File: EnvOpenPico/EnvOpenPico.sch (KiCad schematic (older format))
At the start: 40 parts, among them J2 SKRKAEE020, J3 2.54mm header 01x20, J4 2.54mm header 01x20, J5 Conn_01x03_Male, U1 TPS63002, U3 RP2040, X1 XO 32 12Mhz 3225 seiko

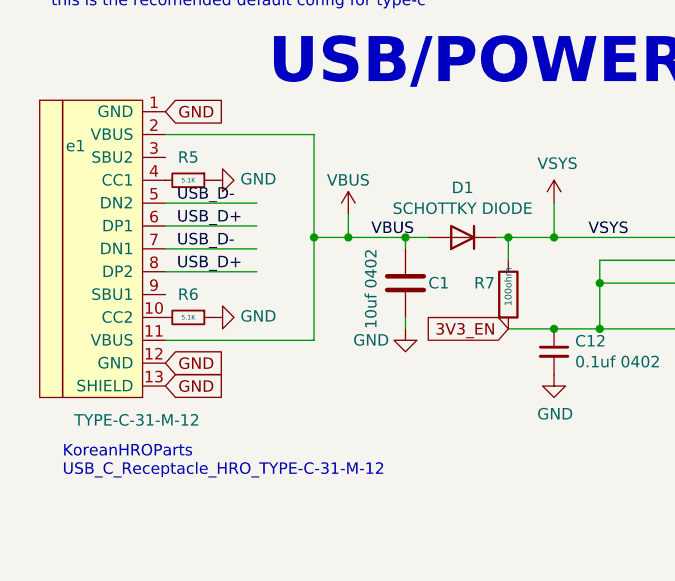
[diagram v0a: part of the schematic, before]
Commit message: small corrections and added a couple test points.
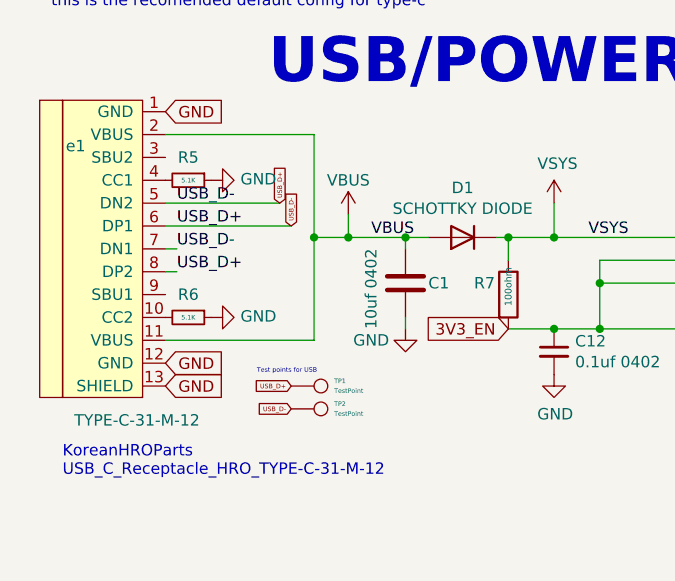
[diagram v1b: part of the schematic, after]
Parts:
- added TP1, TP2: TestPoint, TestPoint:TestPoint_Pad_1.0x1.0mm, symbol Connector:TestPoint
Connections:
- net USB_D- is gone; now on net USB_D+: R4.1, e1.5 (DN2), e1.7 (DN1)
- net USB_D+: now also TP1.1, TP2.1
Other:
- note added: "Test points for USB"
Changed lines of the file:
@@
 	1750 1300 1750 1750
 Connection ~ 1900 1750
-Wire Wire Line
-	1100 1600 1500 1600
-Wire Wire Line
-	1100 1700 1500 1700
 Text Label 1150 1900 0    50   ~ 0
 USB_D+
 Text Label 1150 1800 0    50   ~ 0
 USB_D-
-Wire Wire Line
-	1100 1800 1500 1800
-Wire Wire Line
-	1100 1900 1500 1900
 Wire Wire Line
 	1750 1750 1750 2200
@@
 Wire Wire Line
 	14600 5200 14100 5200
+Text GLabel 1600 1600 1    20   Input ~ 0
+USB_D+
+Text GLabel 1650 1700 1    20   Input ~ 0
+USB_D-
+Text GLabel 1650 2500 0    20   Input ~ 0
+USB_D-
+Text GLabel 1650 2400 0    20   Input ~ 0
+USB_D+
+$Comp
+L Connector:TestPoint TP1
+U 1 1 6102353C
+P 1650 2400
+F 0 "TP1" V 1628 2588 20  0000 L CNN
+F 1 "TestPoint" V 1671 2588 20  0000 L CNN
+F 2 "TestPoint:TestPoint_Pad_1.0x1.0mm" H 1850 2400 50  0001 C CNN
+F 3 "~" H 1850 2400 50  0001 C CNN
+	1    1650 2400
+	0    1    1    0
+$EndComp
+$Comp
+L Connector:TestPoint TP2
+U 1 1 61023F3F
+P 1650 2500
+F 0 "TP2" V 1628 2688 20  0000 L CNN
+F 1 "TestPoint" V 1671 2688 20  0000 L CNN
+F 2 "TestPoint:TestPoint_Pad_1.0x1.0mm" H 1850 2500 50  0001 C CNN
+F 3 "~" H 1850 2500 50  0001 C CNN
+	1    1650 2500
+	0    1    1    0
+$EndComp
+Wire Wire Line
+	1100 1600 1600 1600
+Wire Wire Line
+	1100 1700 1650 1700
+Wire Wire Line
+	1100 1800 1150 1800
+Wire Wire Line
+	1100 1900 1150 1900
+Text Notes 1500 2350 0    20   ~ 0
+Test points for USB
 $EndSCHEMATC

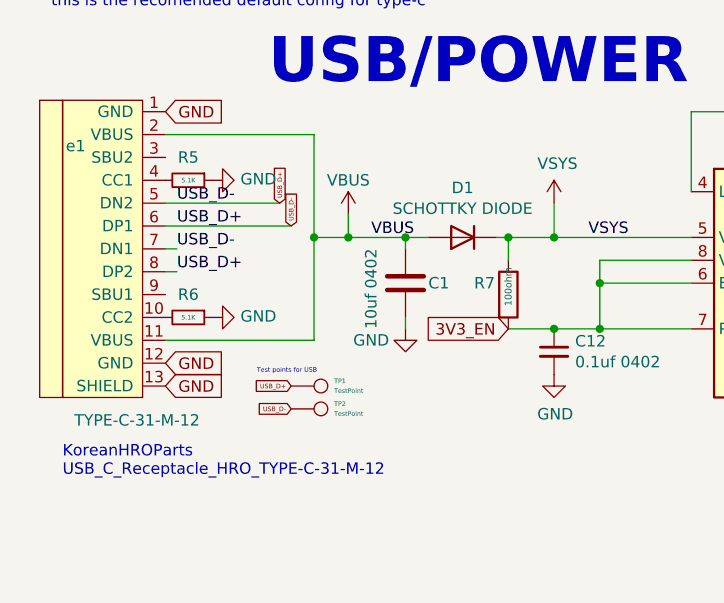
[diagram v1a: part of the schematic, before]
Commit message: corrected reveresed usb debug pads, added gnd debug pad and incremented revision number.
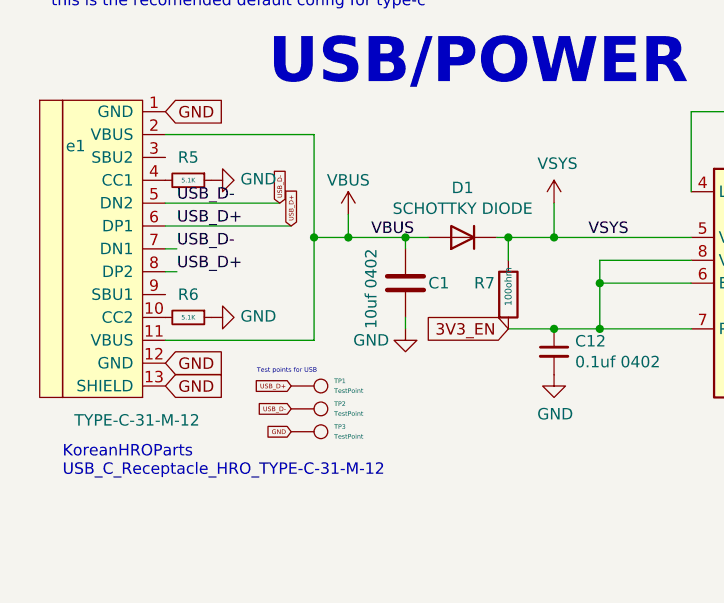
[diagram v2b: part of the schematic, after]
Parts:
- added TP3: TestPoint, TestPoint:TestPoint_Pad_1.0x1.0mm, symbol Connector:TestPoint
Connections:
- net GND: now also TP3.1
- net USB_D+: no longer R4.1, TP2.1, e1.5 (DN2), e1.7 (DN1)
- new net USB_D-: R4.1, TP2.1, e1.5 (DN2), e1.7 (DN1)
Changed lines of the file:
@@
 Wire Wire Line
 	14600 5200 14100 5200
+Text GLabel 1650 1700 1    20   Input ~ 0
+USB_D+
 Text GLabel 1600 1600 1    20   Input ~ 0
-USB_D+
-Text GLabel 1650 1700 1    20   Input ~ 0
 USB_D-
 Text GLabel 1650 2500 0    20   Input ~ 0
@@
 $EndComp
 Wire Wire Line
-	1100 1600 1600 1600
-Wire Wire Line
-	1100 1700 1650 1700
-Wire Wire Line
 	1100 1800 1150 1800
 Wire Wire Line
@@
 Text Notes 1500 2350 0    20   ~ 0
 Test points for USB
+$Comp
+L Connector:TestPoint TP3
+U 1 1 60FFE72F
+P 1650 2600
+F 0 "TP3" V 1628 2788 20  0000 L CNN
+F 1 "TestPoint" V 1671 2788 20  0000 L CNN
+F 2 "TestPoint:TestPoint_Pad_1.0x1.0mm" H 1850 2600 50  0001 C CNN
+F 3 "~" H 1850 2600 50  0001 C CNN
+	1    1650 2600
+	0    1    1    0
+$EndComp
+Text GLabel 1650 2600 0    20   Input ~ 0
+GND
+Wire Wire Line
+	1100 1600 1600 1600
+Wire Wire Line
+	1100 1700 1650 1700
 $EndSCHEMATC

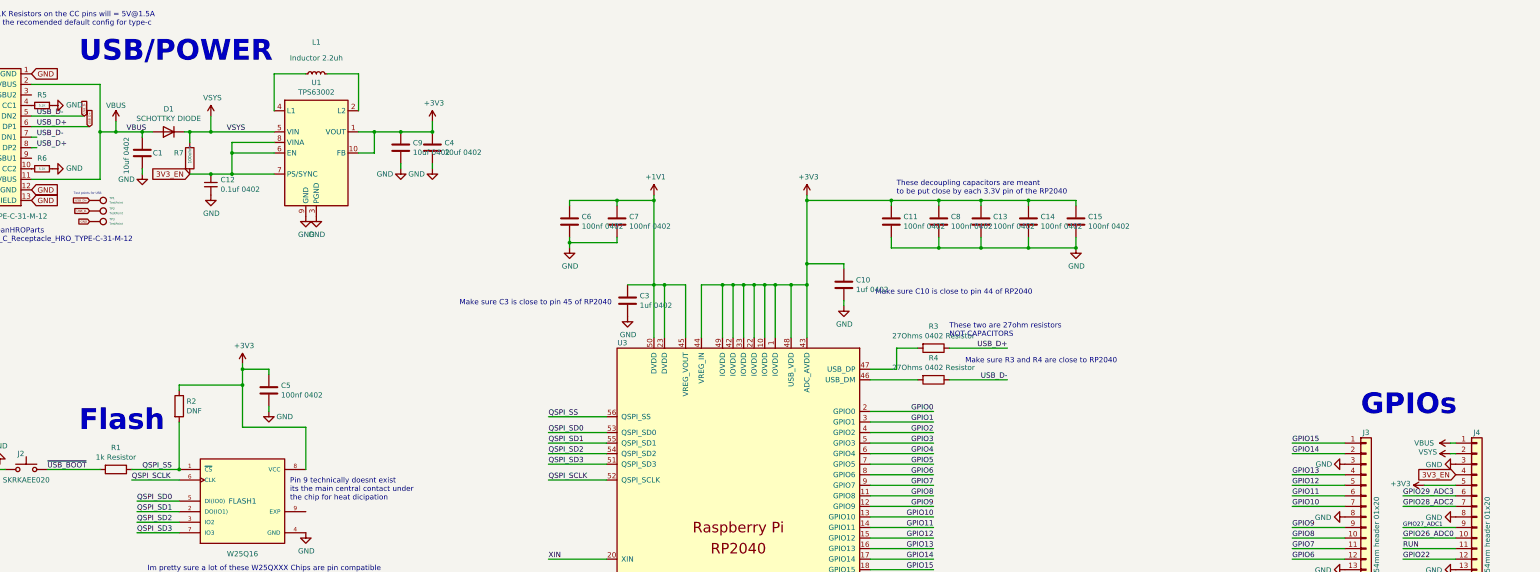
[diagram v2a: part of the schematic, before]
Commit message: Hopefully implemented ADC_VREF Correctly on dip40 and pico verrsion
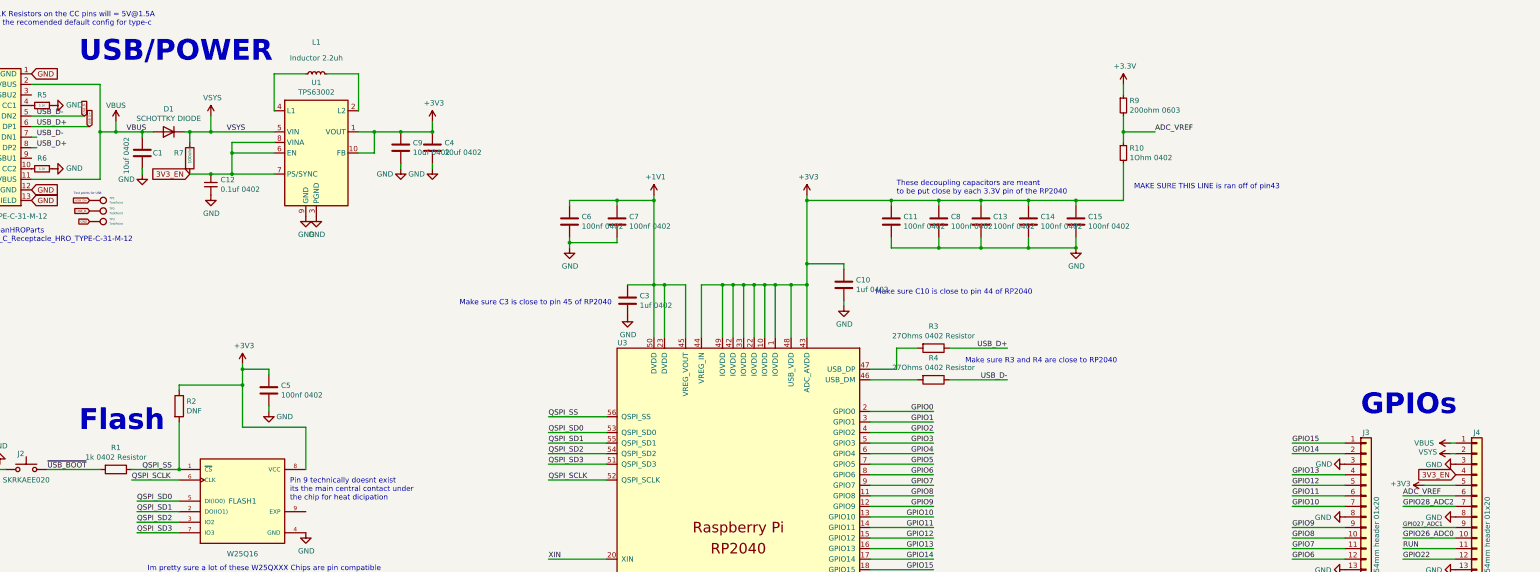
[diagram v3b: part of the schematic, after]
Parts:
- added R10: 1Ohm 0402, Resistor_SMD:R_0402_1005Metric, symbol Device:R_Small
- added R9: 200ohm 0603, Resistor_SMD:R_0603_1608Metric, symbol Device:R_Small
- R1: value 1k Resistor -> 1k 0402 Resistor
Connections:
- net +3V3: now also R10.2, R9.1
- net GPIO29_ADC3: no longer J4.6 (Pin_6)
- new net ADC_VREF: J4.6 (Pin_6), R10.1, R9.2
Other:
- note added: "MAKE SURE THIS LINE is ran off of pin43"
- note removed: "These two are 27ohm resistors \nNOT CAPACITORS"
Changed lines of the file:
@@
 P 1900 4950
 F 0 "R1" V 1693 4950 50  0000 C CNN
-F 1 "1k Resistor" V 1784 4950 50  0000 C CNN
+F 1 "1k 0402 Resistor" V 1784 4950 50  0000 C CNN
 F 2 "Capacitor_SMD:C_0402_1005Metric" V 1830 4950 50  0001 C CNN
 F 3 "" H 1900 4950 50  0001 C CNN
@@
 Text Notes 2200 6000 0    50   ~ 0
 Im pretty sure a lot of these W25QXXX Chips are pin compatible\nDont quote me on that
-Text Notes 9800 3700 0    50   ~ 0
-These two are 27ohm resistors \nNOT CAPACITORS
 Text Notes 650  2800 0    50   ~ 0
 KoreanHROParts \nUSB_C_Receptacle_HRO_TYPE-C-31-M-12
@@
 	1    0    0    -1
 $EndComp
-Text Label 14100 5200 0    50   ~ 0
-GPIO29_ADC3
 Wire Wire Line
 	14600 5200 14100 5200
@@
 Wire Wire Line
 	1100 1700 1650 1700
+Wire Wire Line
+	11000 2400 11450 2400
+Wire Wire Line
+	11450 2400 11450 2050
+Connection ~ 11000 2400
+$Comp
+L Device:R_Small R10
+U 1 1 610441D8
+P 11450 1950
+F 0 "R10" H 11509 1996 50  0000 L CNN
+F 1 "1Ohm 0402" H 11509 1905 50  0000 L CNN
+F 2 "Resistor_SMD:R_0402_1005Metric" H 11450 1950 50  0001 C CNN
+F 3 "~" H 11450 1950 50  0001 C CNN
+	1    11450 1950
+	1    0    0    -1
+$EndComp
+$Comp
+L Device:R_Small R9
+U 1 1 61044B24
+P 11450 1500
+F 0 "R9" H 11509 1546 50  0000 L CNN
+F 1 "200ohm 0603" H 11509 1455 50  0000 L CNN
+F 2 "Resistor_SMD:R_0603_1608Metric" H 11450 1500 50  0001 C CNN
+F 3 "~" H 11450 1500 50  0001 C CNN
+	1    11450 1500
+	1    0    0    -1
+$EndComp
+$Comp
+L power:+3.3V #PWR013
+U 1 1 61045079
+P 11450 1300
+F 0 "#PWR013" H 11450 1150 50  0001 C CNN
+F 1 "+3.3V" H 11465 1473 50  0000 C CNN
+F 2 "" H 11450 1300 50  0001 C CNN
+F 3 "" H 11450 1300 50  0001 C CNN
+	1    11450 1300
+	1    0    0    -1
+$EndComp
+Wire Wire Line
+	11450 1300 11450 1400
+Wire Wire Line
+	11450 1600 11450 1750
+Wire Wire Line
+	11450 1750 11750 1750
+Connection ~ 11450 1750
+Wire Wire Line
+	11450 1750 11450 1850
+Text Label 11750 1750 0    50   ~ 0
+ADC_VREF
+Text Notes 11550 2300 0    50   ~ 0
+MAKE SURE THIS LINE is ran off of pin43
+Text Label 14100 5200 0    50   ~ 0
+ADC_VREF
 $EndSCHEMATC

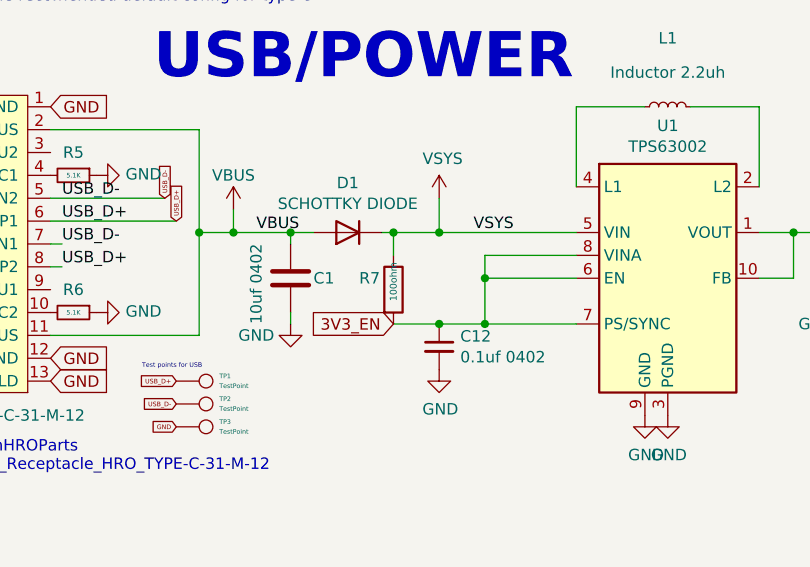
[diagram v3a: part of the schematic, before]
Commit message: updated readme and corrected a capacitor placement.
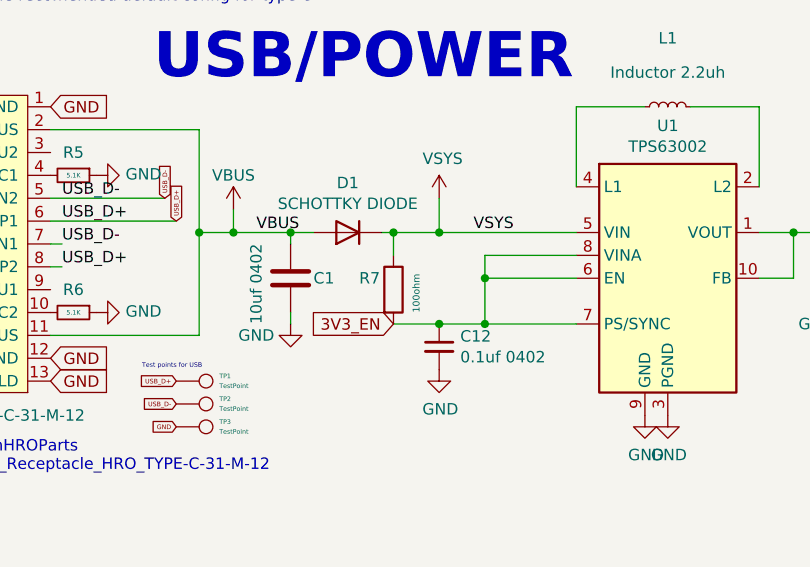
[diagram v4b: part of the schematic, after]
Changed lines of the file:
@@
 P 2600 2000
 F 0 "R7" H 2450 2050 50  0000 L CNN
-F 1 "100ohm" V 2600 1950 30  0000 L CNN
+F 1 "100ohm" V 2700 1900 30  0000 L CNN
 F 2 "Resistor_SMD:R_0402_1005Metric" V 2530 2000 50  0001 C CNN
 F 3 "" H 2600 2000 50  0001 C CNN

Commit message: bit of a redesign.
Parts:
- added C16, C18: 100nf 0402, Capacitor_SMD:C_0402_1005Metric, symbol Device:C
- C1: value 10uf 0402 -> 10uf 0603 6.3V; footprint Capacitor_SMD:C_0402_1005Metric -> Capacitor_SMD:C_0603_1608Metric
- FLASH1: footprint Package_SO:SOIJ-8_5.3x5.3mm_P1.27mm -> Package_SON:SON-8-1EP_3x2mm_P0.5mm_EP1.4x1.6mm
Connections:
- net +3V3: now also C16.1, C18.1
- net GND: now also C16.2, C18.2
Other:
- note added: "this is for factory testing\n\nalways pull this to ground"
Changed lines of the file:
@@
 P 2150 1950
 F 0 "C1" H 2250 1950 50  0000 L CNN
-F 1 "10uf 0402" V 2000 1750 50  0000 L CNN
-F 2 "Capacitor_SMD:C_0402_1005Metric" H 2188 1800 50  0001 C CNN
+F 1 "10uf 0603 6.3V" V 2000 1800 20  0000 L CNN
+F 2 "Capacitor_SMD:C_0603_1608Metric" H 2188 1800 50  0001 C CNN
 F 3 "" H 2150 1950 50  0001 C CNN
 	1    2150 1950
-	1    0    0    -1
-$EndComp
-$Comp
-L Device:C C4
-U 1 1 5F0930A1
-P 4900 1900
-F 0 "C4" H 5015 1946 50  0000 L CNN
-F 1 "10uf 0402" H 5015 1855 50  0000 L CNN
-F 2 "Capacitor_SMD:C_0402_1005Metric" H 4938 1750 50  0001 C CNN
-F 3 "" H 4900 1900 50  0001 C CNN
-	1    4900 1900
 	1    0    0    -1
 $EndComp
@@
 Wire Wire Line
 	2150 2100 2150 2150
-$Comp
-L power:GND #PWR010
-U 1 1 5F0A1049
-P 4900 2100
-F 0 "#PWR010" H 4900 1850 50  0001 C CNN
-F 1 "GND" H 4750 2050 50  0000 C CNN
-F 2 "" H 4900 2100 50  0001 C CNN
-F 3 "" H 4900 2100 50  0001 C CNN
-	1    4900 2100
-	1    0    0    -1
-$EndComp
-Wire Wire Line
-	4900 2050 4900 2100
 Wire Wire Line
 	8450 3000 8800 3000
@@
 	1    0    0    -1
 $EndComp
-Text Notes 9100 3300 0    50   ~ 0
+Text Notes 8950 3050 0    50   ~ 0
 Make sure C10 is close to pin 44 of RP2040
 Text Notes 6600 3400 2    50   ~ 0
@@
 F 0 "FLASH1" H 3100 5250 50  0000 C CNN
 F 1 "W25Q16" H 3100 4750 50  0000 C CNN
-F 2 "Package_SO:SOIJ-8_5.3x5.3mm_P1.27mm" H 3100 5250 50  0001 L BNN
+F 2 "Package_SON:SON-8-1EP_3x2mm_P0.5mm_EP1.4x1.6mm" H 3100 5250 50  0001 L BNN
 F 3 "" H 3100 5250 50  0001 L BNN
 	1    3100 5250
@@
 P 4600 1900
 F 0 "C9" H 4715 1946 50  0000 L CNN
-F 1 "10uf 0402" H 4715 1855 50  0000 L CNN
+F 1 "10uf 0402" H 4550 1900 20  0000 L CNN
 F 2 "Capacitor_SMD:C_0402_1005Metric" H 4638 1750 50  0001 C CNN
 F 3 "" H 4600 1900 50  0001 C CNN
@@
 Wire Wire Line
 	4900 1750 4600 1750
-Connection ~ 4900 1750
-Wire Wire Line
-	4200 1750 4350 1750
 Connection ~ 4600 1750
-Wire Wire Line
-	4200 1950 4350 1950
-Wire Wire Line
-	4350 1950 4350 1750
-Connection ~ 4350 1750
-Wire Wire Line
-	4350 1750 4600 1750
 $Comp
 L power:GND #PWR05
@@
 	1100 1700 1650 1700
 Wire Wire Line
-	11000 2400 11450 2400
+	11000 2400 11400 2400
 Wire Wire Line
 	11450 2400 11450 2050
@@
 Text Label 14100 5200 0    50   ~ 0
 ADC_VREF
+Wire Wire Line
+	4200 1750 4350 1750
+Wire Wire Line
+	4200 1950 4350 1950
+Wire Wire Line
+	4350 1950 4350 1750
+Connection ~ 4350 1750
+Wire Wire Line
+	4350 1750 4600 1750
+$Comp
+L Device:C C4
+U 1 1 6109C424
+P 4900 1900
+F 0 "C4" H 5015 1946 50  0000 L CNN
+F 1 "10uf 0402" H 4850 1900 20  0000 L CNN
+F 2 "Capacitor_SMD:C_0402_1005Metric" H 4938 1750 50  0001 C CNN
+F 3 "" H 4900 1900 50  0001 C CNN
+	1    4900 1900
+	1    0    0    -1
+$EndComp
+$Comp
+L power:GND #PWR0114
+U 1 1 6109CAB2
+P 4900 2100
+F 0 "#PWR0114" H 4900 1850 50  0001 C CNN
+F 1 "GND" H 4750 2050 50  0000 C CNN
+F 2 "" H 4900 2100 50  0001 C CNN
+F 3 "" H 4900 2100 50  0001 C CNN
+	1    4900 2100
+	1    0    0    -1
+$EndComp
+Connection ~ 4900 1750
+Wire Wire Line
+	4900 2050 4900 2100
+$Comp
+L Device:C C16
+U 1 1 6118E37D
+P 11400 2600
+F 0 "C16" H 11515 2646 50  0000 L CNN
+F 1 "100nf 0402" H 11515 2555 50  0000 L CNN
+F 2 "Capacitor_SMD:C_0402_1005Metric" H 11438 2450 50  0001 C CNN
+F 3 "" H 11400 2600 50  0001 C CNN
+	1    11400 2600
+	1    0    0    -1
+$EndComp
+$Comp
+L Device:C C18
+U 1 1 6118EBF5
+P 11750 2600
+F 0 "C18" H 11865 2646 50  0000 L CNN
+F 1 "100nf 0402" H 11865 2555 50  0000 L CNN
+F 2 "Capacitor_SMD:C_0402_1005Metric" H 11788 2450 50  0001 C CNN
+F 3 "" H 11750 2600 50  0001 C CNN
+	1    11750 2600
+	1    0    0    -1
+$EndComp
+Wire Wire Line
+	11400 2400 11400 2450
+Connection ~ 11400 2400
+Wire Wire Line
+	11400 2400 11450 2400
+Wire Wire Line
+	11400 2750 11400 2850
+Wire Wire Line
+	11400 2850 11000 2850
+Wire Wire Line
+	11750 2750 11750 2850
+Wire Wire Line
+	11400 2850 11750 2850
+Connection ~ 11400 2850
+Wire Wire Line
+	11750 2400 11750 2450
+Connection ~ 11450 2400
+Wire Wire Line
+	11450 2400 11750 2400
+Text Notes 6200 7900 0    50   ~ 0
+this is for factory testing\n\nalways pull this to ground
 $EndSCHEMATC
